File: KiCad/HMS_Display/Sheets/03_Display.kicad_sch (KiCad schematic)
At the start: 8 parts, among them U2 OLED_SSD1306_SPI_0.96, U23 DISPLAY1_POWER_SOCKET, U24 DISPLAY1_DATA_SOCKET, U25 DISPLAY2_POWER_SOCKET, U28 DISPLAY2_DATA_SOCKET, U29 OLED_SSD1306_SPI_0.96

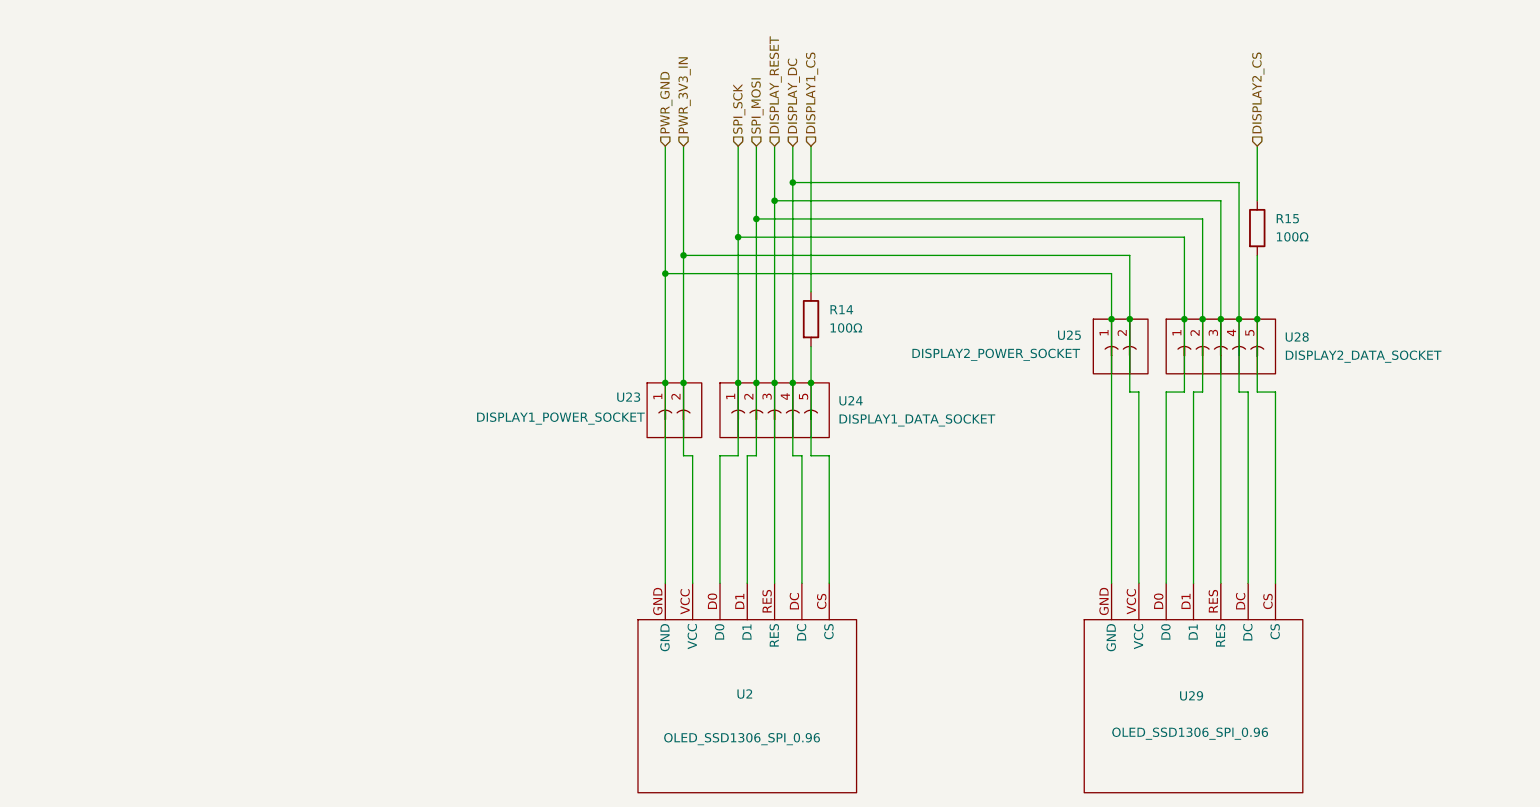
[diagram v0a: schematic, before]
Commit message: HMS_Diaply Kicad schematics and PCB
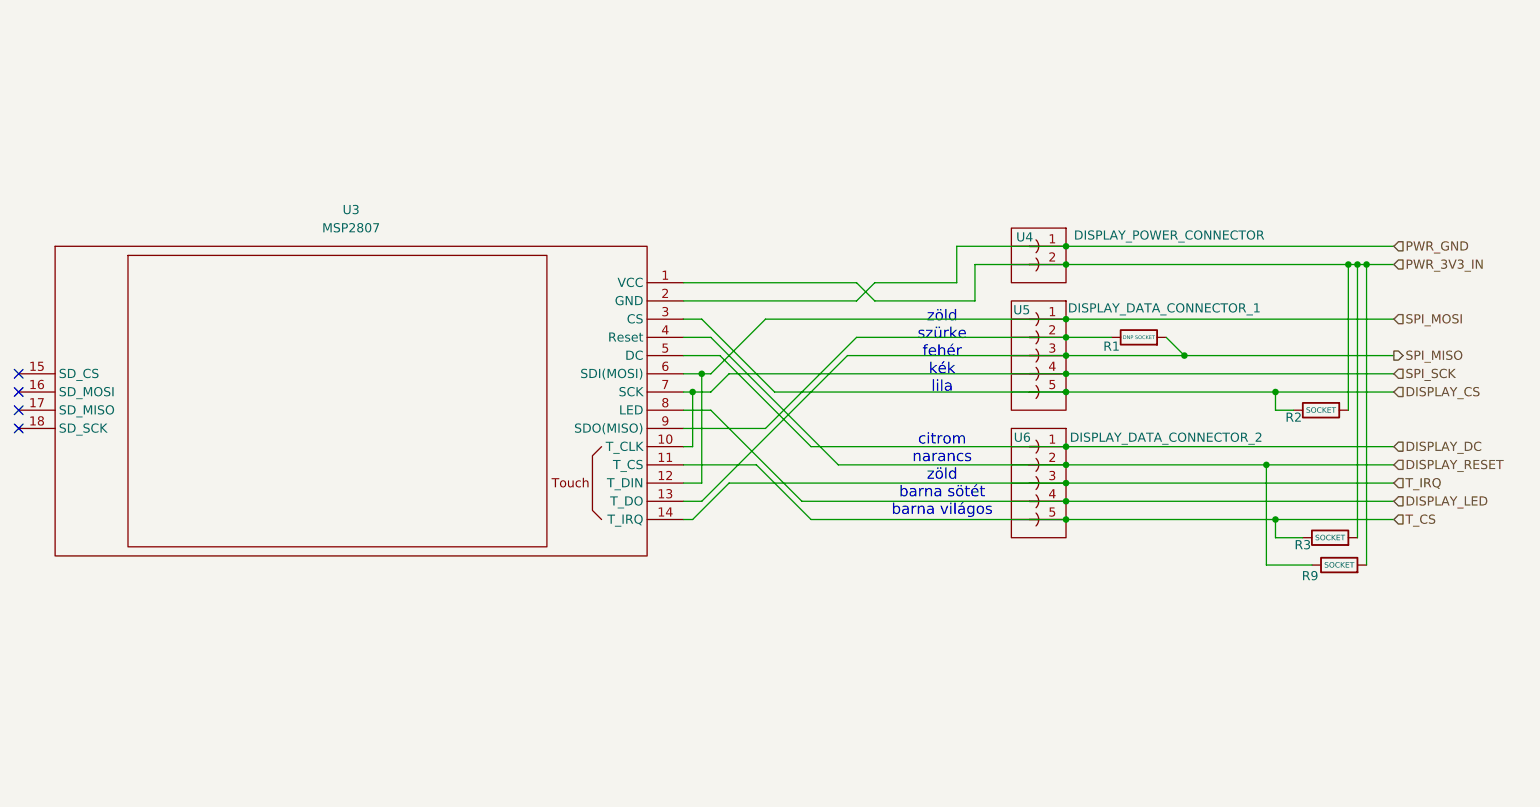
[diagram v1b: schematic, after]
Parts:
- removed R15: 100Ω, Resistor_THT:R_Axial_DIN0207_L6.3mm_D2.5mm_P7.62mm_Horizontal, symbol Device:R
- removed U2, U29: OLED_SSD1306_SPI_0.96, symbol HMS_Symbols:OLED_SSD1306_SPI_0.96
- removed U25: DISPLAY2_POWER_SOCKET, Connector_JST:JST_XH_B2B-XH-A_1x02_P2.50mm_Vertical, symbol HMS_Symbols:CONN_JST_PH_2P
- removed U28: DISPLAY2_DATA_SOCKET, Connector_JST:JST_XH_B5B-XH-A_1x05_P2.50mm_Vertical, symbol HMS_Symbols:CONN_JST_PH_5P
- added R1: DNP SOCKET, Resistor_THT:R_Axial_DIN0207_L6.3mm_D2.5mm_P7.62mm_Horizontal, symbol Device:R
- added R3, R9: SOCKET, Resistor_THT:R_Axial_DIN0207_L6.3mm_D2.5mm_P7.62mm_Horizontal, symbol Device:R
- added U3: MSP2807, symbol HMS_Symbols:MSP2807
- added U6: DISPLAY_DATA_CONNECTOR_2, Connector_JST:JST_XH_B5B-XH-A_1x05_P2.50mm_Vertical, symbol HMS_Symbols:CONN_JST_PH_5P
- R2: renamed from R14; value 100Ω -> SOCKET
- U4: renamed from U23; value DISPLAY1_POWER_SOCKET -> DISPLAY_POWER_CONNECTOR
- U5: renamed from U24; value DISPLAY1_DATA_SOCKET -> DISPLAY_DATA_CONNECTOR_1
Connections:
- net DISPLAY1_CS is gone; now on net DISPLAY_CS: R2.1
- net DISPLAY_DC: now also U3.5 (DC), U6.1; no longer U5.4
- net DISPLAY_RESET: now also R9.1, U3.4 (Reset), U6.2; no longer U5.3
- net PWR_3V3_IN: now also R2.2, R3.2, R9.2, U3.1 (VCC)
- net PWR_GND: now also U3.2 (GND)
- net SPI_MOSI: now also U5.1, U3.12 (T_DIN), U3.6 (SDI(MOSI)); no longer U5.2
- net SPI_SCK: now also U5.4, U3.10 (T_CLK), U3.7 (SCK); no longer U5.1
- net DISPLAY_CS: now reaches U5.5
- net DISPLAY_CS: now also U3.3 (CS); no longer R2.2
- new net: R1.1, U3.9 (SDO(MISO)), U5.2
- new net DISPLAY_LED: U3.8 (LED), U6.4
- new net SPI_MISO: R1.2, U3.13 (T_DO), U5.3
- new net T_CS: R3.1, U3.11 (T_CS), U6.5
- new net T_IRQ: U3.14 (T_IRQ), U6.3
- no-connect marks 0 -> 4
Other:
- note added: "zöld szürke fehér kék lila citrom narancs zöld barna sötét barna világos"
- moved on the sheet: R2, U4, U5
